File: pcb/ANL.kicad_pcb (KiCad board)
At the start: 2 copper layers, 77.2 x 50.8 mm, 70 parts, among them J1 Conn_01x10_Socket, J10 Conn_01x02_Socket, J11 Conn_01x02_Socket, J12 Conn_01x02_Socket, J13 Conn_01x02_Socket, J14 Conn_01x02_Socket, J15 Conn_01x02_Socket, J16 Conn_01x02_Socket, J17 Conn_01x02_Socket, J18 Conn_01x02_Socket, J19 Conn_01x02_Socket, J2 Conn_01x02_Pin, J20 Conn_01x02_Socket, J21 Conn_01x02_Socket, J22 Conn_01x02_Socket, J23 Conn_01x02_Socket, J24 Conn_01x02_Socket, J25 Conn_01x02_Socket, J26 Conn_01x02_Socket, J27 Conn_01x02_Socket, J28 Conn_01x02_Socket, J29 Conn_01x02_Socket, J3 Conn_01x10_Socket, J30 Conn_01x02_Socket, J31 Conn_01x02_Socket, J32 Conn_01x02_Socket, J33 Conn_01x02_Socket, J4 Conn_02x02_Counter_Clockwise, J5 Conn_02x02_Counter_Clockwise, J6 Conn_02x02_Counter_Clockwise, J7 Conn_02x02_Counter_Clockwise, J8 Conn_02x02_Counter_Clockwise, J9 Conn_02x02_Counter_Clockwise, U1 4081, U2 4081

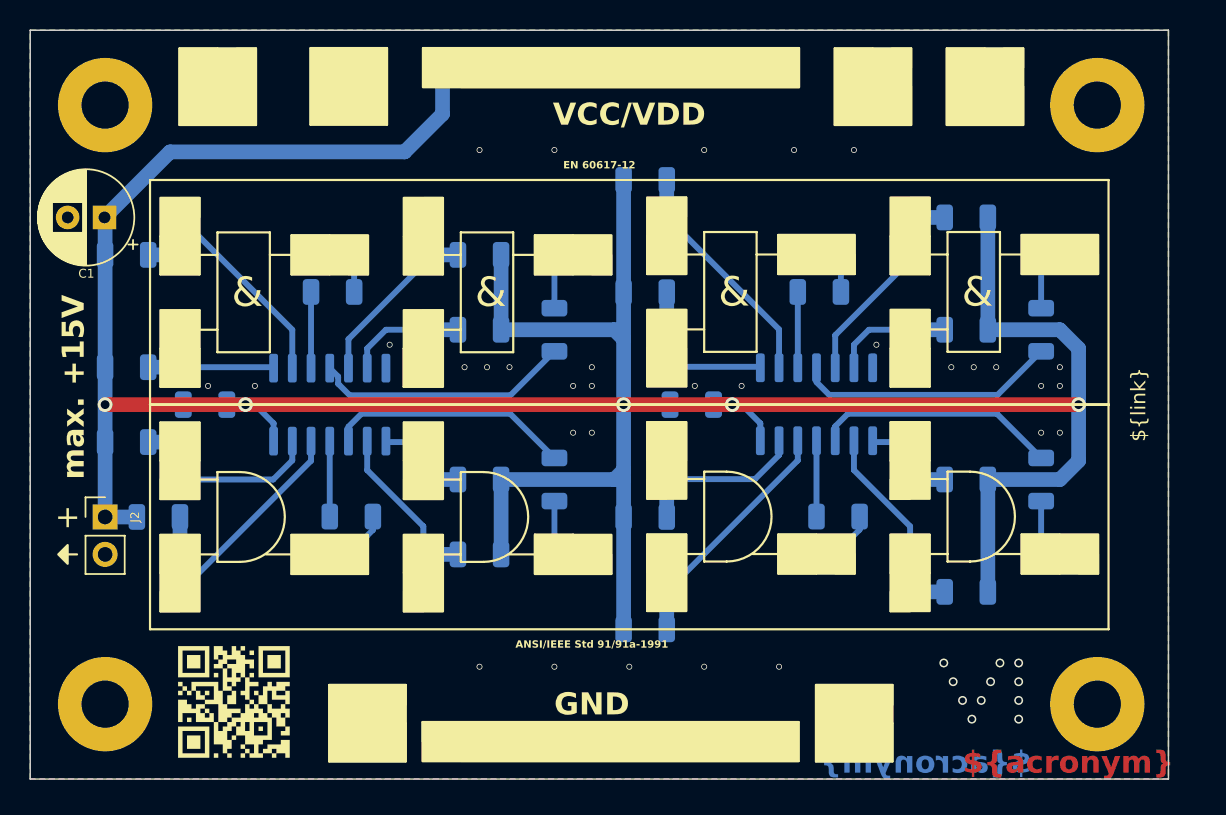
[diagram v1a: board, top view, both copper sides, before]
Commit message: Adapt edge cuts and dimensioning
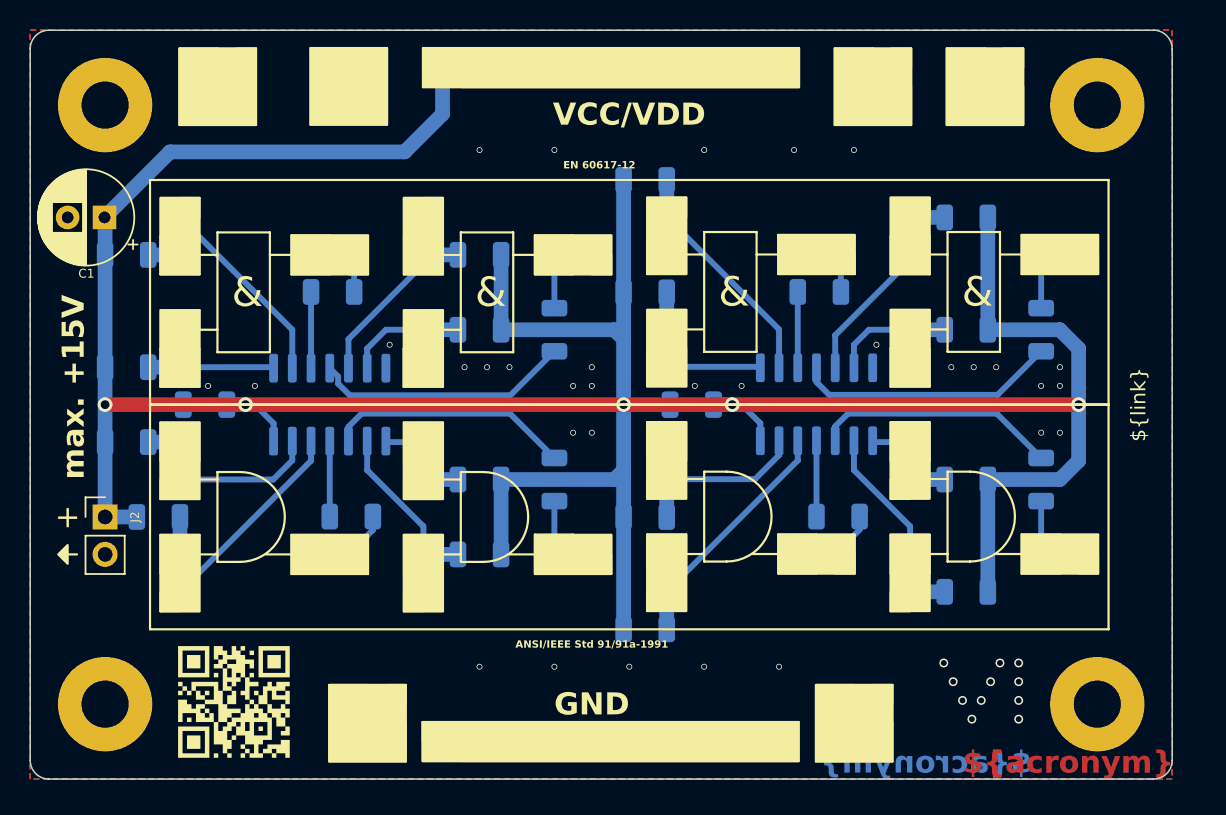
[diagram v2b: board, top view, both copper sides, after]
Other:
- board size 77.2 x 50.8 mm -> 77.5 x 50.8 mm
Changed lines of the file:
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@@
   (gr_rect (start 137.1 110.43) (end 142.3 113.09)
     (stroke (width 0.15) (type solid)) (fill solid) (layer "F.SilkS"))
-  (gr_rect (start 119.38 76.2) (end 196.596 127)
-    (stroke (width 0.1) (type default)) (fill none) (layer "Edge.Cuts"))
+  (gr_line (start 119.38 125.73) (end 119.38 77.47)
+    (stroke (width 0.1) (type default)) (layer "Edge.Cuts"))
+  (gr_arc (start 120.65 127) (mid 119.751974 126.628026) (end 119.38 125.73)
+    (stroke (width 0.1) (type default)) (layer "Edge.Cuts"))
+  (gr_line (start 120.65 76.2) (end 195.58 76.2)
+    (stroke (width 0.1) (type default)) (layer "Edge.Cuts"))
+  (gr_arc (start 195.58 76.2) (mid 196.478026 76.571974) (end 196.85 77.47)
+    (stroke (width 0.1) (type default)) (layer "Edge.Cuts"))
+  (gr_line (start 195.58 127) (end 120.65 127)
+    (stroke (width 0.1) (type default)) (layer "Edge.Cuts"))
+  (gr_arc (start 119.38 77.47) (mid 119.751974 76.571974) (end 120.65 76.2)
+    (stroke (width 0.1) (type default)) (layer "Edge.Cuts"))
+  (gr_line (start 196.85 77.47) (end 196.85 125.73)
+    (stroke (width 0.1) (type default)) (layer "Edge.Cuts"))
+  (gr_arc (start 196.85 125.73) (mid 196.478026 126.628026) (end 195.58 127)
+    (stroke (width 0.1) (type default)) (layer "Edge.Cuts"))
   (gr_text "${acronym}" (at 182.626 126.746) (layer "F.Cu")
     (effects (font (size 1.5 1.5) (thickness 0.3) bold) (justify left bottom))
@@
   (dimension (type aligned) (layer "Dwgs.User")
     (pts (xy 119.38 76.2) (xy 119.38 127))
-    (height 1.27)
-    (gr_text "50.80" (at 116.96 101.6 90) (layer "Dwgs.User")
+    (height 3.81)
+    (gr_text "50.80" (at 114.42 101.6 90) (layer "Dwgs.User")
       (effects (font (size 1 1) (thickness 0.15)))
     )
@@
   )
   (dimension (type aligned) (layer "Dwgs.User")
-    (pts (xy 119.38 76.2) (xy 196.596 76.2))
-    (height -1.27)
-    (gr_text "77.22" (at 157.988 73.78) (layer "Dwgs.User")
+    (pts (xy 124.46 81.28) (xy 124.46 76.2))
+    (height -6.35)
+    (gr_text "5.08" (at 116.96 78.74 90) (layer "Dwgs.User")
+      (effects (font (size 1 1) (thickness 0.15)))
+    )
+    (format (prefix "") (suffix "") (units 3) (units_format 0) (precision 2))
+    (style (thickness 0.15) (arrow_length 1.27) (text_position_mode 0) (extension_height 0.58642) (extension_offset 0.5) keep_text_aligned)
+  )
+  (dimension (type aligned) (layer "Dwgs.User")
+    (pts (xy 124.46 81.28) (xy 119.38 81.28))
+    (height 6.35)
+    (gr_text "5.08" (at 121.92 73.78) (layer "Dwgs.User")
+      (effects (font (size 1 1) (thickness 0.15)))
+    )
+    (format (prefix "") (suffix "") (units 3) (units_format 0) (precision 2))
+    (style (thickness 0.15) (arrow_length 1.27) (text_position_mode 0) (extension_height 0.58642) (extension_offset 0.5) keep_text_aligned)
+  )
+  (dimension (type aligned) (layer "Dwgs.User")
+    (pts (xy 119.38 74.93) (xy 196.85 74.93))
+    (height -2.54)
+    (gr_text "77.47" (at 158.115 71.24) (layer "Dwgs.User")
       (effects (font (size 1 1) (thickness 0.15)))
     )
@@
       (pts
         (xy 119.38 76.2)
-        (xy 196.596 76.2)
-        (xy 196.596 127)
+        (xy 196.85 76.2)
+        (xy 196.85 127)
         (xy 119.38 127)
       )

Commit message: Add reverse polarity protection
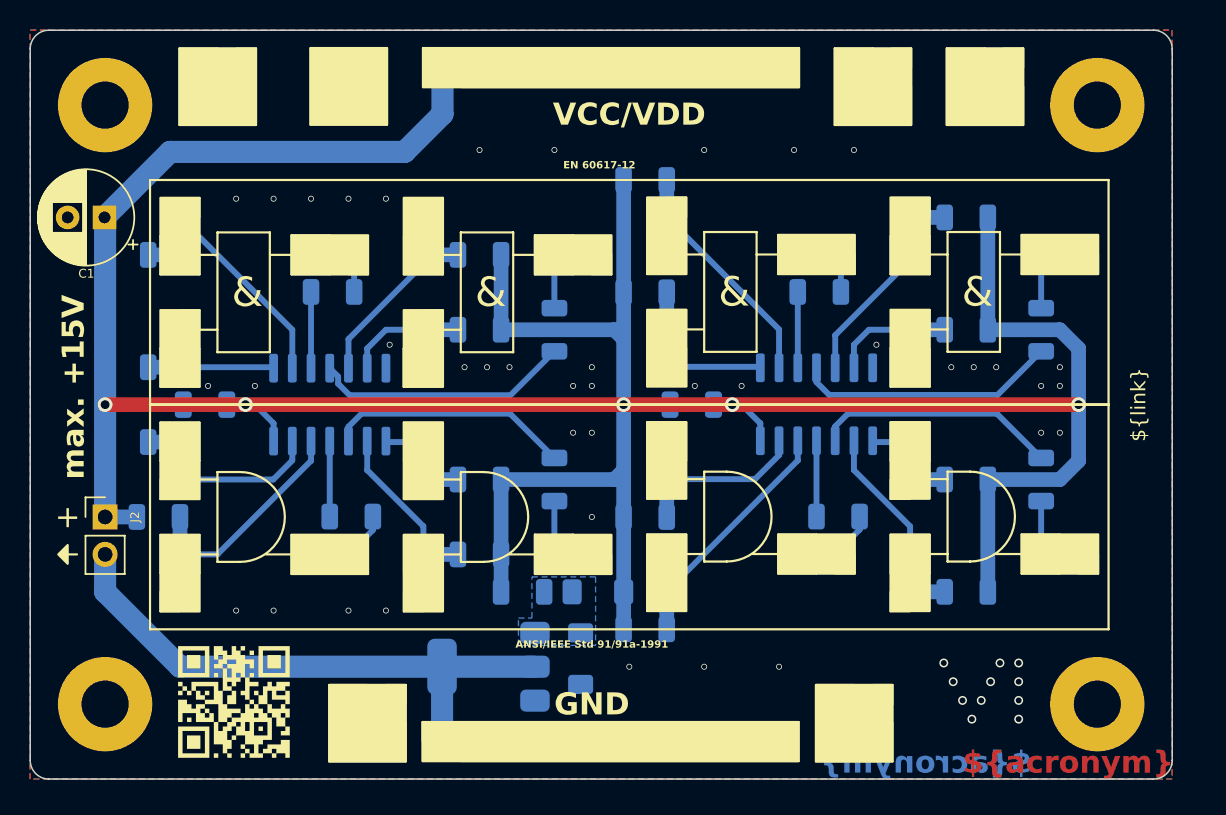
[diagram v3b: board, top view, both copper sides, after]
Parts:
- added D1: BAT43, Diode_SMD:D_MiniMELF, B.Cu at (157.9, 114.3)
- added D2: BZ5V1, Diode_SMD:D_MiniMELF, B.Cu at (156.7, 118.8)
- added Q1: BUK7880-55A, Package_TO_SOT_SMD:SOT-223-3_TabPin2, B.Cu at (150.5, 119.4)
- added R25: 1k, Resistor_SMD:R_1206_3216Metric, B.Cu at (152.8, 114.3)
- moved FID3 37.0 mm to (167.6, 84.1)
- moved FID2 20.4 mm to (167.6, 116.8)
- moved FID1 9.86 mm to (175.3, 116.8)
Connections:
- J2 pad 2: GND -> Net-(J2-Pin_2)
- J3 pad 1: GND -> Net-(J2-Pin_2)
- J3 pad 10: GND -> Net-(J2-Pin_2)
- J3 pad 2: GND -> Net-(J2-Pin_2)
- J3 pad 3: GND -> Net-(J2-Pin_2)
- J3 pad 4: GND -> Net-(J2-Pin_2)
- J3 pad 5: GND -> Net-(J2-Pin_2)
- J3 pad 6: GND -> Net-(J2-Pin_2)
- J3 pad 7: GND -> Net-(J2-Pin_2)
- J3 pad 8: GND -> Net-(J2-Pin_2)
- J3 pad 9: GND -> Net-(J2-Pin_2)
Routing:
- net Net-(J2-Pin_2): track 0.00 -> 38.9 mm
- net VCC: track 222.6 -> 225.1 mm
- net Net-(J17-Pin_1): track 19.0 -> 17.9 mm
- net GND: vias 43 -> 51
- added copper zone on B.Cu, net Net-(D1-A)
- added copper zone on B.Cu, net Net-(J2-Pin_2)
